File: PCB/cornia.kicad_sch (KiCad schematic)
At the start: 78 parts, among them J1 Conn_01x01_Pin, SW1 SW_Push, SW10 SW_Push, SW11 SW_Push, SW12 SW_Push, SW13 SW_Push, SW14 SW_Push, SW15 SW_Push, SW16 SW_Push, SW17 SW_Push, SW18 SW_Push, SW19 SW_Push, SW2 SW_Push, SW20 SW_Push, SW21 SW_Push, SW3 SW_Push, SW4 SW_Push, SW5 SW_Push, SW6 SW_Push, SW7 SW_Push, SW8 SW_Push, SW9 SW_Push, U1 RP2040-ProMicro, U2 TRRS

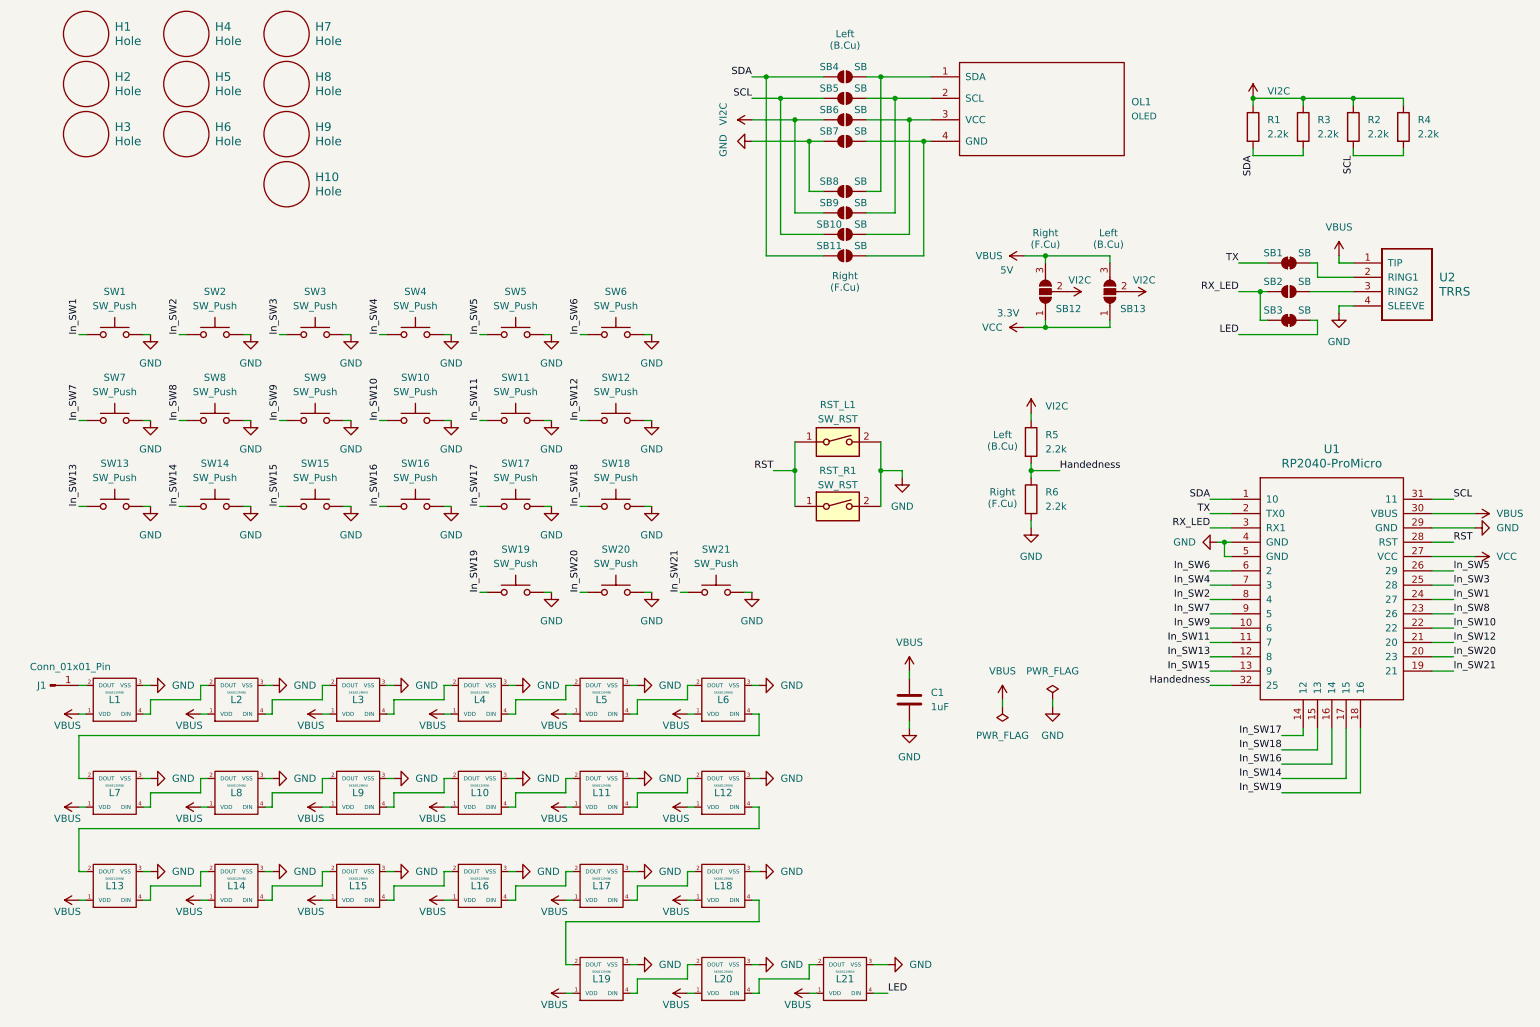
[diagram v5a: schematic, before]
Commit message: [PCB] Multiple fix based on v1RC2 board bring-up
- Reduce RST thermal relief width
- Update SB silkscreen
- Update TRRS silkscreen
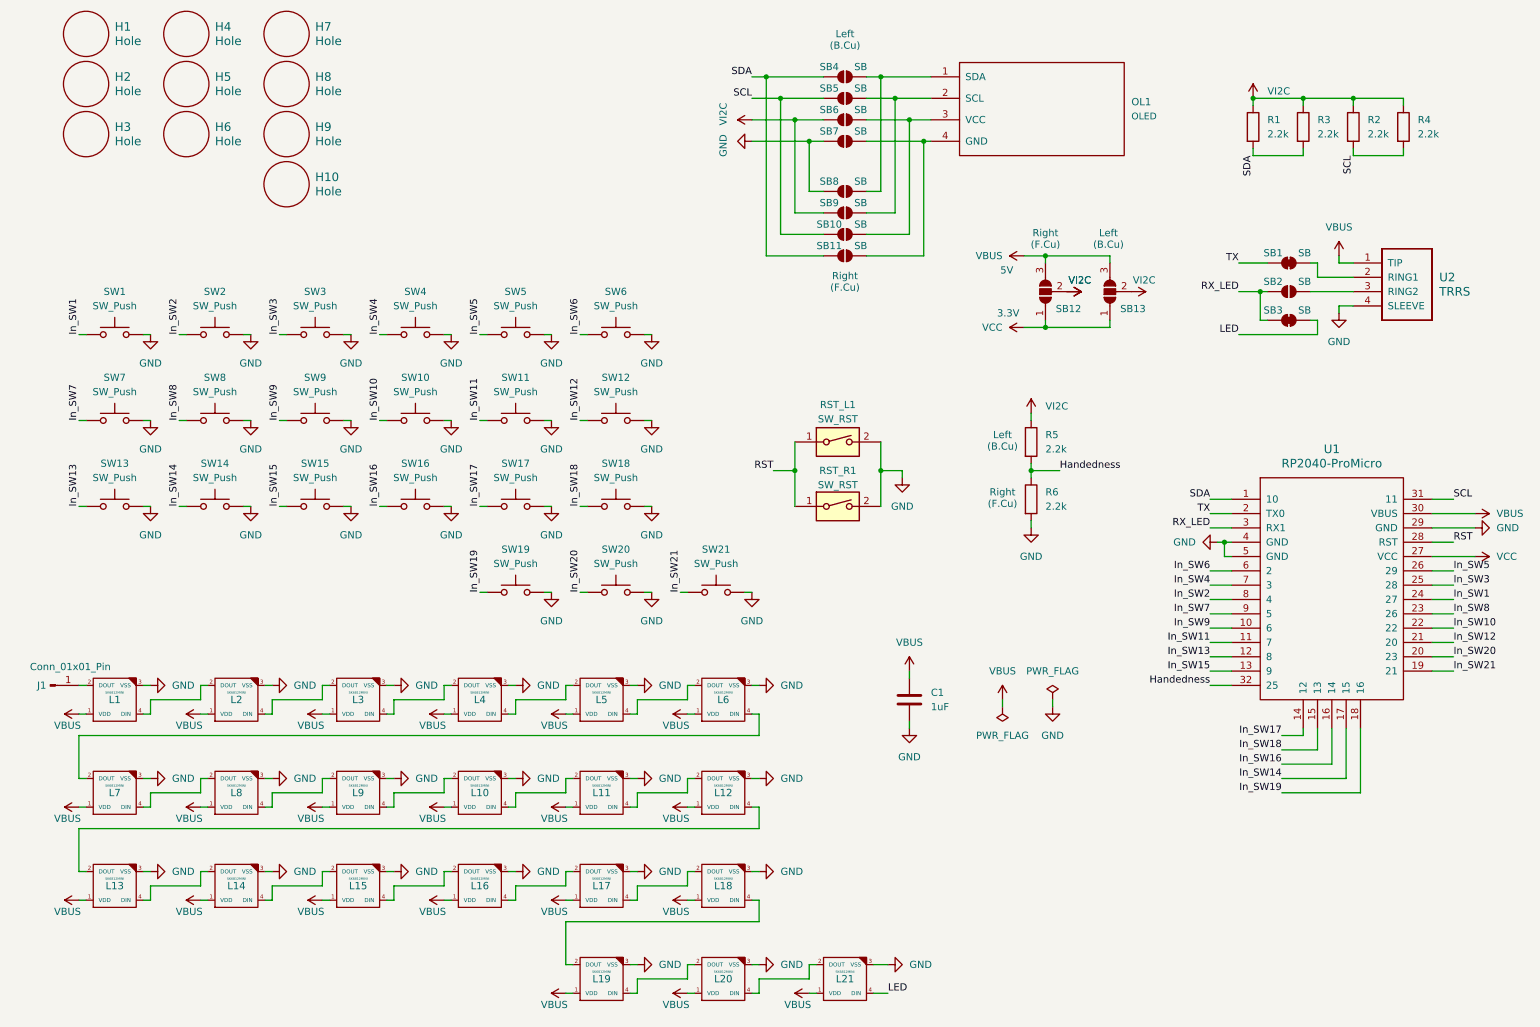
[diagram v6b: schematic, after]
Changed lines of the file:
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@@
+	)
+	(symbol
+		(lib_id "power:VBUS")
+		(at 198.12 68.58 270)
+		(unit 1)
+		(exclude_from_sim no)
+		(in_bom yes)
+		(on_board yes)
+		(dnp no)
+		(property "Reference" "#PWR0101"
+			(at 194.31 68.58 0)
+			(effects
+				(font
+					(size 1.27 1.27)
+				)
+				(hide yes)
+			)
+		)
+		(property "Value" "VI2C"
+			(at 198.374 66.548 90)
+			(effects
+				(font
+					(size 1.27 1.27)
+				)
+				(justify left)
+			)
+		)
+		(property "Footprint" ""
+			(at 198.12 68.58 0)
+			(effects
+				(font
+					(size 1.27 1.27)
+				)
+				(hide yes)
+			)
+		)
+		(property "Datasheet" ""
+			(at 198.12 68.58 0)
+			(effects
+				(font
+					(size 1.27 1.27)
+				)
+				(hide yes)
+			)
+		)
+		(property "Description" "Power symbol creates a global label with name \"VBUS\""
+			(at 198.12 68.58 0)
+			(effects
+				(font
+					(size 1.27 1.27)
+				)
+				(hide yes)
+			)
+		)
+		(pin "1"
+		)
+		(instances
+			(project "cornia"
+				(path "/fba9d1ab-287c-4388-b412-675aea5ffe31"
+					(reference "#PWR0101")
+					(unit 1)
+				)
+			)
+		)
 	)
 	(symbol

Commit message: [PCB] Swap TX RX pins
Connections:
- net RX_LED renamed TX_LED
- net TX_LED: now also U1.2 (TX0); no longer U1.3 (RX1)
- net TX renamed RX
- net RX: now also U1.3 (RX1); no longer U1.2 (TX0)
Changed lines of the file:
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@@
 		)
 	)
-	(label "RX_LED"
+	(label "RX"
+		(at 228.6 63.5 180)
+		(fields_autoplaced yes)
+		(effects
+			(font
+				(size 1.27 1.27)
+			)
+			(justify right bottom)
+		)
+	)
+	(label "RX"
 		(at 223.52 110.49 180)
-		(fields_autoplaced yes)
-		(effects
-			(font
-				(size 1.27 1.27)
-			)
-			(justify right bottom)
-		)
-	)
-	(label "TX"
-		(at 228.6 63.5 180)
 		(fields_autoplaced yes)
 		(effects
@@
 		)
 	)
-	(label "TX"
-		(at 223.52 107.95 180)
-		(fields_autoplaced yes)
-		(effects
-			(font
-				(size 1.27 1.27)
-			)
-			(justify right bottom)
-		)
-	)
 	(label "SCL"
 		(at 142.24 34.29 180)
@@
 		)
 	)
-	(label "RX_LED"
+	(label "TX_LED"
 		(at 228.6 68.58 180)
 		(fields_autoplaced yes)
@@
 		(fields_autoplaced yes)
 		(effects
+			(font
+				(size 1.27 1.27)
+			)
+			(justify right bottom)
+		)
+	)
+	(label "TX_LED"
+		(at 223.52 107.95 180)
+		(fields_autoplaced yes)
+		(effects

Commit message: [PCB] Swap RST_L1 & RST_R1 to match their respective sides
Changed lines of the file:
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@@
+	(text "Left\n(B.Cu)"
+		(exclude_from_sim no)
+		(at 157.48 85.09 0)
+		(effects
+			(font
+				(size 1.27 1.27)
+			)
+		)
+	)
+	(text "Right\n(F.Cu)"
+		(exclude_from_sim no)
+		(at 157.48 112.268 0)
+		(effects
+			(font
+				(size 1.27 1.27)
+			)
+		)
+	)
 	(text "Left\n(B.Cu)"
 		(exclude_from_sim no)
